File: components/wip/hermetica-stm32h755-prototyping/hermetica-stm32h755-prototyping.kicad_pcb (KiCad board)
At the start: 4 copper layers, 74.9 x 110.5 mm, 233 parts, among them J1 CONNECTOR-DEBUG-SPECIFIC-ARM, J10 Conn_01x01, J100 Conn_01x01, J101 Conn_01x01, J102 Conn_01x01, J103 Conn_01x01, J104 Conn_01x01, J105 Conn_01x01, J106 Conn_01x01, J107 Conn_01x01, J108 Conn_01x01, J109 Conn_01x01, J11 Conn_01x01, J111 Conn_01x01, J112 Conn_01x01, J113 Conn_01x01, J114 Conn_01x01, J115 Conn_01x01, J116 Conn_01x01, J117 Conn_01x01, J118 Conn_01x01, J119 Conn_01x01, J12 Conn_01x01, J120 Conn_01x01, J121 Conn_01x01, J122 Conn_01x01, J123 Conn_01x01, J124 Conn_01x01, J125 Conn_01x01, J126 Conn_01x01, J127 Conn_01x01, J128 Conn_01x01, J129 Conn_01x01, J13 Conn_01x01, J130 Conn_01x01, J131 Conn_01x01, J132 Conn_01x01, J133 Conn_01x01, J134 Conn_01x01, J135 Conn_01x01, J136 Conn_01x01, J137 Conn_01x01, J138 Conn_01x01, J139 Conn_01x01, J14 Conn_01x01, J140 Conn_01x01, J141 Conn_01x01, J142 Conn_01x01, J143 Conn_01x01, J144 Conn_01x01, J145 Conn_01x01, J146 Conn_01x01, J147 Conn_01x01, J148 Conn_01x01, J149 Conn_01x01, J15 Conn_01x01, J16 Conn_01x01, J17 Conn_01x01, J18 Conn_01x01, J19 Conn_01x01, J2 Conn_01x01, J20 Conn_01x01, J21 Conn_01x01, J22 Conn_01x01, J23 Conn_01x01, J24 Conn_01x01, J25 Conn_01x01, J26 Conn_01x01, J27 Conn_01x01, J28 Conn_01x01, J29 Conn_01x01, J3 Conn_01x01, J30 Conn_01x01, J31 Conn_01x01, J32 Conn_01x01, J33 Conn_01x01, J34 Conn_01x01, J35 Conn_01x01, J36 Conn_01x01, J37 Conn_01x01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

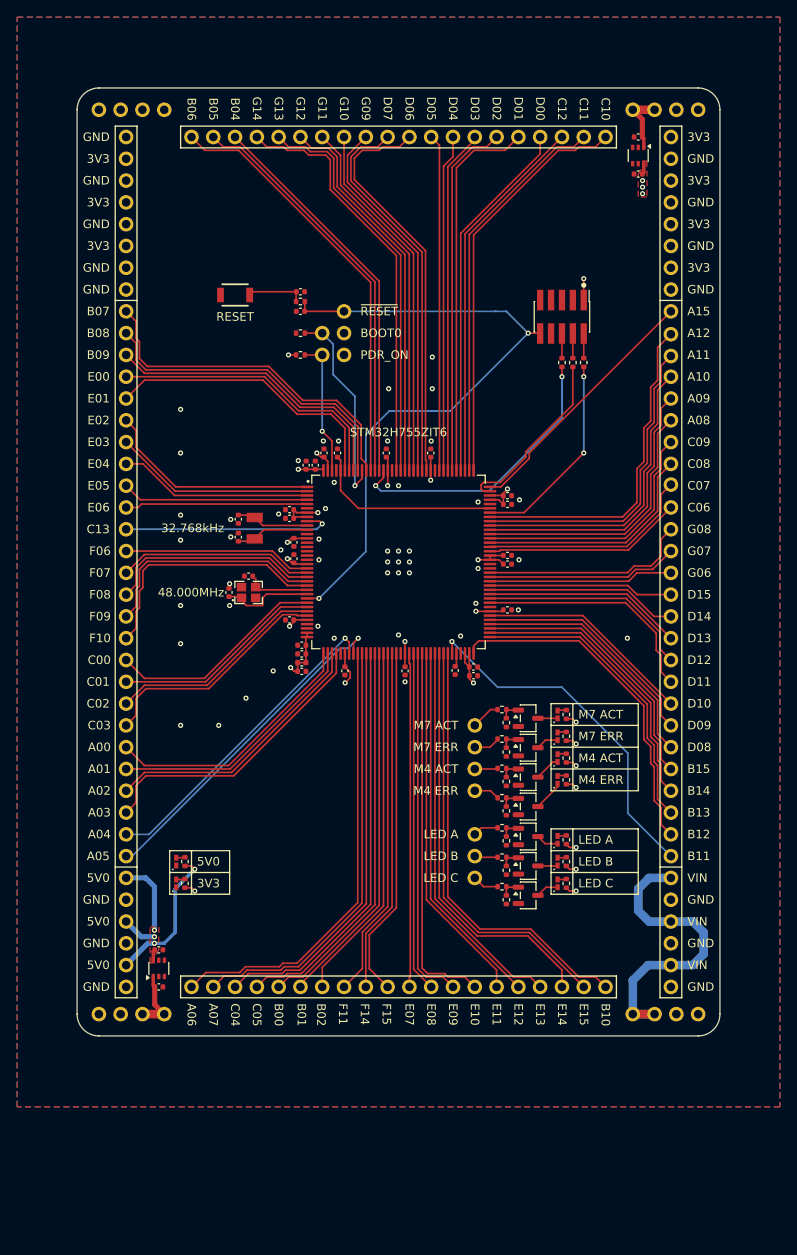
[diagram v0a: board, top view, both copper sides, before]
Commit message: STM32H755ZIT6 dev board
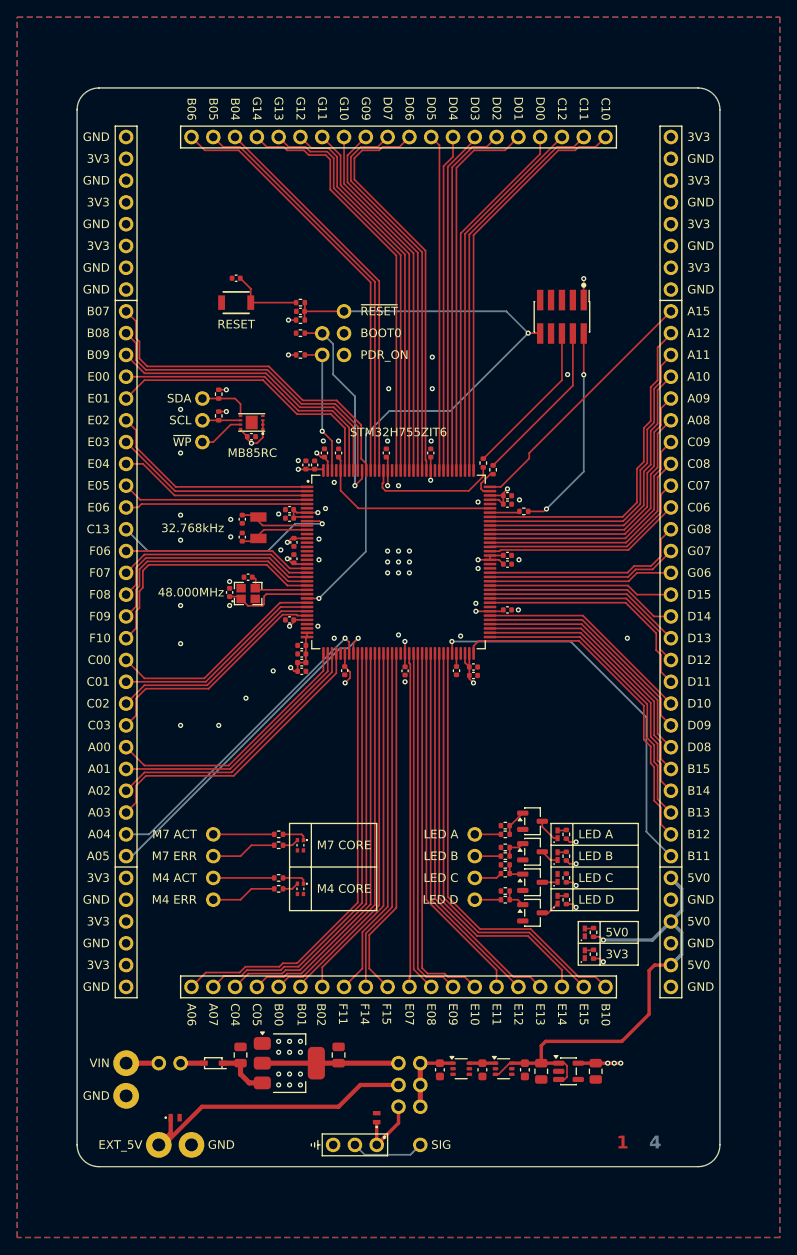
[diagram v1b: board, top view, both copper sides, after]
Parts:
- removed C39, C40, C41, C42: 100nF, djStandard:C_0402_1005Metric
- removed C43, C44, C45, C46: 2.2uF, djStandard:C_0402_1005Metric
- removed J10, J11, J12, J13, J14, J15, J16, J33, J36, J39, J7, J8, J9: Conn_01x01, djStandard:CONNECTOR-PCB-HANDSOLDER-01X01-FEMALE
- removed J143, J144, J145: Conn_01x01, djStandard:CONNECTOR-PCB-HANDSOLDER-01X01-MALE
- removed LED7, LED8, LED9: KINGBRIGHT-LED-0402-ORANGE, djStandard:KINGBRIGHT-LED-APHHS1005-0402
- removed Q5, Q6, Q7: DIODESINC-MMBT4401-7-F-SOT-23-3, Package_TO_SOT_SMD:SOT-23-3
- removed R24, R27: 47K, djStandard:R_0402_1005Metric
- removed R25, R28: 10K, djStandard:R_0402_1005Metric
- removed R26: ?, djStandard:R_0402_1005Metric
- removed R29: 22R, djStandard:R_0402_1005Metric
- removed U2: LM66100DCK, Package_TO_SOT_SMD:SOT-363_SC-70-6
- added C12: 4.7uF, djStandard:C_0402_1005Metric, F.Cu at (-10.8, -11.3)
- added C13: 100nF, djStandard:C_0402_1005Metric, F.Cu at (-8.64, -12.7)
- added C14: 100nF, djStandard:C_0402_1005Metric, F.Cu at (12.7, -6.73)
- added C15: 100nF, djStandard:C_0402_1005Metric, F.Cu at (12.7, 0.25)
- added C16: 100nF, djStandard:C_0402_1005Metric, F.Cu at (-6.27, 12.7)
- added C17: 100nF, djStandard:C_0402_1005Metric, F.Cu at (8.74, 13.2)
- added C18: 100nF, djStandard:C_0402_1005Metric, F.Cu at (-12.7, -5.11)
- added C3: 2.2uF, djStandard:C_0402_1005Metric, F.Cu at (-17.5, 1.78)
- added C6: 2.2uF, djStandard:C_0402_1005Metric, F.Cu at (-18.2, -2.90)
- added C7: 2.2uF, djStandard:C_0402_1005Metric, F.Cu at (6.76, 12.7)
- added C8: 2.2uF, djStandard:C_0402_1005Metric, F.Cu at (-6.99, -12.7)
- added C9: 10uF, djStandard:C_0402_1005Metric, F.Cu at (-11.3, 12.8)
- added D1: BAT60JFILM, djStandard:STM-BAT60JFILM-SOT-323-2, F.Cu at (-21.6, 58.4)
- added D2: ESDA7P60-1U1M, djStandard:STM-ESDA7P60-1U1M, F.Cu at (-2.54, 64.8)
- added D3: ESDA7P60-1U1M, djStandard:STM-ESDA7P60-1U1M, F.Cu at (-26.0, 64.8)
- added H1: MountingHole_Pad, djStandard:MountingHole_1.5mm, F.Cu at (-31.8, 58.4)
- added H2: MountingHole_Pad, djStandard:MountingHole_1.5mm, F.Cu at (-31.8, 62.2)
- added H3: MountingHole_Pad, djStandard:MountingHole_1.5mm, F.Cu at (-27.9, 67.9)
- added H4: MountingHole_Pad, djStandard:MountingHole_1.5mm, F.Cu at (-24.1, 67.9)
- added IC1: FUJITSU-MB85RC64TAPN, djStandard:FUJITSU-MB85RC64TAPN-SON8, F.Cu at (-17.1, -16.3)
- added J110: Conn_01x01, djStandard:CONNECTOR-PCB-HANDSOLDER-01X01-FEMALE, F.Cu at (-31.8, -11.4)
- added J150: Conn_01x01, djStandard:CONNECTOR-PCB-HANDSOLDER-01X01-FEMALE, F.Cu at (-21.6, 39.4)
- added J151: Conn_01x01, djStandard:CONNECTOR-PCB-HANDSOLDER-01X01-FEMALE, F.Cu at (-21.6, 36.8)
- added J70: Conn_01x01, djStandard:CONNECTOR-PCB-HANDSOLDER-01X01-FEMALE, F.Cu at (31.8, 34.3)
- added J71: Conn_01x01, djStandard:CONNECTOR-PCB-HANDSOLDER-01X01-FEMALE, F.Cu at (31.8, 31.8)
- added J72: Conn_01x01, djStandard:CONNECTOR-PCB-HANDSOLDER-01X01-FEMALE, F.Cu at (31.8, 29.2)
- added JP1: Jumper_2_Open, djStandard:CONNECTOR-PCB-HANDSOLDER-01X02-MALE, F.Cu at (-8.89, -24.1)
- added JP4: Jumper_2_Open, djStandard:CONNECTOR-PCB-HANDSOLDER-01X02-MALE, F.Cu at (0.00, 58.4)
- added JP5: Jumper_2_Open, djStandard:CONNECTOR-PCB-HANDSOLDER-01X02-MALE, F.Cu at (0.00, 61.0)
- added JP6: Jumper_2_Open, djStandard:CONNECTOR-PCB-HANDSOLDER-01X02-MALE, F.Cu at (0.00, 63.5)
- added LED10: APHB1608CGKSURKC, djStandard:KINGBRIGHT-APHB1608CGKSURKC, F.Cu at (-11.4, 33.0)
- added LED11: APHB1608CGKSURKC, djStandard:KINGBRIGHT-APHB1608CGKSURKC, F.Cu at (-11.4, 38.1)
- added R30: ?, djStandard:R_0402_1005Metric, F.Cu at (-14.0, 33.0)
- added R31: ?, djStandard:R_0402_1005Metric, F.Cu at (-14.0, 31.8)
- added R32: ?, djStandard:R_0402_1005Metric, F.Cu at (-14.0, 38.1)
- added R33: ?, djStandard:R_0402_1005Metric, F.Cu at (-14.0, 36.8)
- added U3: LM66100DCK, Package_TO_SOT_SMD:SOT-363_SC-70-6, F.Cu at (7.30, 59.1)
- added U4: LM66100DCK, Package_TO_SOT_SMD:SOT-363_SC-70-6, F.Cu at (12.3, 59.1)
- added U5: AP2112K-3.3, Package_TO_SOT_SMD:SOT-23-5, F.Cu at (19.8, 59.4)
- C1: value 1uF -> 22nF
- C10: value 10pF -> 1uF
- C11: value 22nF -> 100nF
- C2: value 1uF -> 10pF
- C31: value 4.7uF -> 10uF; footprint djStandard:C_0402_1005Metric -> djStandard:C_0805_2012Metric
- C32: value 100nF -> 10uF; footprint djStandard:C_0402_1005Metric -> djStandard:C_0805_2012Metric
- C34, C35, C36: value 100nF -> 1uF; footprint djStandard:C_0402_1005Metric -> djStandard:C_0603_1608Metric
- C37, C38: value 2.2uF -> 1uF; footprint djStandard:C_0402_1005Metric -> djStandard:C_0805_2012Metric
- C4, C5: value 1uF -> 2.2uF
- J1: value CONNECTOR-DEBUG-SPECIFIC-ARM -> Conn_01x01; footprint djStandard:PinHeader_2x05_P1.27mm_Vertical_SMD -> djStandard:CONNECTOR-PCB-HANDSOLDER-01X01-FEMALE
- J128, J129, J136, J137, J138, J139, J140, J141, J142, J147, J148, J149: footprint djStandard:CONNECTOR-PCB-HANDSOLDER-01X01-MALE -> djStandard:CONNECTOR-PCB-HANDSOLDER-01X01-FEMALE; moved to F.Cu
- J146: value Conn_01x01 -> DRONE-SERVO-HEADER; footprint djStandard:CONNECTOR-PCB-HANDSOLDER-01X01-MALE -> djStandard:CONNECTOR-SERVO-VERTICAL; moved to F.Cu
- J17: value Conn_01x01 -> CONNECTOR-DEBUG-SPECIFIC-ARM; footprint djStandard:CONNECTOR-PCB-HANDSOLDER-01X01-FEMALE -> djStandard:PinHeader_2x05_P1.27mm_Vertical_SMD
- LED2: value KINGBRIGHT-LED-0402-RED -> KINGBRIGHT-LED-0402-ORANGE
- LED6: value KINGBRIGHT-LED-0402-ORANGE -> KINGBRIGHT-LED-0402-RED
- R1, R3: value ? -> 22R
- R10: value 1K -> ?
- R12, R7: value 47K -> ?
- R13, R16: value 10K -> 47K
- R14: value ? -> 47K
- R17, R20: value ? -> 10K
- R18, R21: value 47K -> 10K
- R22: value 10K -> 20K
- R23: value ? -> 20K
- R4: value 22R -> 10K
- R6: value ? -> 1K
- R8, R9: value 10K -> ?
- SW1: value OMRON-B3U-1000PM -> B3U1000PM
- U1: value LM66100DCK -> LD1117S50TR_SOT223; footprint Package_TO_SOT_SMD:SOT-363_SC-70-6 -> Package_TO_SOT_SMD:SOT-223-3_TabPin2
- Y1: value ABRACON-ABS07-LR-32.768KHZ-6-1-T -> ABRACON-ABM10AIG-48.000MHZ-4Z-T3; footprint djStandard:ABRACON-ABS07-LR -> djStandard:ABRACON-ABM10AIG
- Y2: value ABRACON-ABM10AIG-48.000MHZ-4Z-T3 -> ABRACON-ABS07-LR-32.768KHZ-6-1-T; footprint djStandard:ABRACON-ABM10AIG -> djStandard:ABRACON-ABS07-LR
- moved J147 125.6 mm to (2.54, 67.9), turned to 0 degrees
- moved J146 124.9 mm to (-2.54, 67.9), turned to -90 degrees
- moved U1 113.3 mm to (-12.7, 58.4), turned to 0 degrees
- moved J138 112.3 mm to (-16.5, -49.5), turned to 0 degrees
- moved J136 109.3 mm to (-11.4, -49.5), turned to 0 degrees
- moved J128 109.3 mm to (-3.81, 49.5), turned to 0 degrees
- moved J129 107.6 mm to (-1.27, 49.5), turned to 0 degrees
- moved J119 104.4 mm to (16.5, 49.5)
- moved J118 102.9 mm to (14.0, 49.5)
- moved J117 101.7 mm to (11.4, 49.5)
- moved J121 101.5 mm to (21.6, 49.5)
- moved J60 101.2 mm to (31.8, -39.4)
- moved J116 100.6 mm to (8.89, 49.5)
- moved J115 99.9 mm to (6.35, 49.5)
- moved J97 99.6 mm to (-1.27, -49.5), turned to 0 degrees
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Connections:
- C1 pad 1: /EXT_3V3 -> /mcu/RESET
- C10 pad 1: Net-(C10-Pad1) -> +3V3
- C11 pad 1: /mcu/RESET -> +3V3
- C2 pad 1: /EXT_5V0 -> Net-(C2-Pad1)
- C31 pad 1: +3V3 -> Net-(D1-K)
- C32 pad 1: +3V3 -> Net-(JP4-A)
- C34 pad 1: +3V3 -> 5V_PREDIODE
- C35 pad 1: +3V3 -> Net-(U3-VOUT)
- C36 pad 1: +3V3 -> +5V0
- C37 pad 1: /mcu/VCAP2 -> +5V0
- C38 pad 1: /mcu/VCAP1 -> +3V3
- C4 pad 1: +3V3 -> GND
- C4 pad 2: GND -> Net-(MCU1-OSC_HSE-)
- C5 pad 1: +5V0 -> GND
- C5 pad 2: GND -> Net-(MCU1-OSC_LSE+)
- J1 pad 1: +3V3 -> /mcu/SCL
- J100 pad 1: /mcu/PE13 -> /mcu/PD10
- J101 pad 1: /mcu/PE14 -> /mcu/PD11
- J102 pad 1: /mcu/PE15 -> /mcu/PD12
- J103 pad 1: /mcu/PF06 -> /mcu/PD13
- J104 pad 1: /mcu/PF07 -> /mcu/PD14
- J105 pad 1: /mcu/PF08 -> /mcu/PD15
- J106 pad 1: /mcu/PF09 -> /mcu/PE00
- J107 pad 1: /mcu/PF10 -> /mcu/PE01
- J108 pad 1: /mcu/PF11 -> /mcu/PE02
- J109 pad 1: GND -> /mcu/PE03
- J111 pad 1: /mcu/PG06 -> /mcu/PE05
- J112 pad 1: /mcu/PG07 -> /mcu/PE06
- J113 pad 1: /mcu/PG08 -> /mcu/PE07
- J114 pad 1: /mcu/PG09 -> /mcu/PE08
- J115 pad 1: /mcu/PG10 -> /mcu/PE09
- J116 pad 1: /mcu/PG11 -> /mcu/PE10
- J117 pad 1: /mcu/PG12 -> /mcu/PE11
- J118 pad 1: /mcu/PG13 -> /mcu/PE12
- J119 pad 1: /mcu/PG14 -> /mcu/PE13
- J120 pad 1: /mcu/PA12 -> /mcu/PE14
- J121 pad 1: +3V3 -> /mcu/PE15
- J122 pad 1: GND -> /mcu/PF06
- J123 pad 1: +3V3 -> /mcu/PF07
- J124 pad 1: GND -> /mcu/PF08
- J125 pad 1: GND -> /mcu/PF09
- J126 pad 1: +3V3 -> /mcu/PF10
- J127 pad 1: GND -> /mcu/PF11
- J128 pad 1: GND -> /mcu/PF14
- J129 pad 1: GND -> /mcu/PF15
- J130 pad 1: +5V0 -> /mcu/PG06
- J131 pad 1: +5V0 -> /mcu/PG07
- J132 pad 1: GND -> /mcu/PG08
- J133 pad 1: GND -> /mcu/PG09
- J134 pad 1: GND -> /mcu/PG10
- J135 pad 1: +5V0 -> /mcu/PG11
- J136 pad 1: EXT_VIN -> /mcu/PG12
- J137 pad 1: /EXT_3V3 -> /mcu/PG13
- J138 pad 1: EXT_VIN -> /mcu/PG14
- J139 pad 1: /EXT_3V3 -> /leds/LED_A
- J140 pad 1: GND -> /leds/LED_B
- J141 pad 1: GND -> /leds/LED_C
- J142 pad 1: GND -> /leds/LED_D
- J146 pad 1: GND -> /power/BEC_5V
- J147 pad 1: GND -> /power/BEC_SIGNAL
- J148 pad 1: unconnected-(J148-Pin_1-Pad1) -> /leds/M7_RED
- J149 pad 1: unconnected-(J149-Pin_1-Pad1) -> /leds/M7_GRN
- J17 pad 1: /mcu/PD01 -> +3V3
- J18 pad 1: /mcu/PD00 -> /mcu/PA00
- J19 pad 1: EXT_VIN -> +5V0
- J2 pad 1: /mcu/RESET -> /mcu/SDA
- J20 pad 1: GND -> /mcu/PA01
- J21 pad 1: +3V3 -> +5V0
- J22 pad 1: /mcu/PF14 -> /mcu/PA02
- J23 pad 1: /mcu/PF15 -> +5V0
- J24 pad 1: /mcu/PA00 -> /mcu/PA03
- J25 pad 1: /mcu/PA01 -> /mcu/PA04
- J26 pad 1: /mcu/PA02 -> /mcu/PA05
- J27 pad 1: /mcu/PA03 -> /mcu/PA06
- J28 pad 1: Net-(J28-Pin_1) -> GND
- J29 pad 1: Net-(J29-Pin_1) -> /mcu/PA07
- J3 pad 1: Net-(J3-Pin_1) -> Net-(IC1-WP)
- J30 pad 1: /mcu/PA06 -> GND
- J31 pad 1: /mcu/PA07 -> /mcu/PA08
- J32 pad 1: /mcu/PA08 -> GND
- J34 pad 1: /mcu/PA10 -> /mcu/PA09
- J35 pad 1: /mcu/PB12 -> GND
- J37 pad 1: GND -> /mcu/PA10
- J38 pad 1: /mcu/PB07 -> GND
- J4 pad 1: EXT_VIN -> +3V3
- J40 pad 1: /mcu/PB00 -> /mcu/PA11
- J41 pad 1: /mcu/PB01 -> GND
- J42 pad 1: /mcu/PB02 -> /mcu/PA12
- J43 pad 1: /mcu/PB04 -> GND
- J44 pad 1: /mcu/PB13 -> GND
- J46 pad 1: Net-(J46-Pin_1) -> +3V3
- J47 pad 1: /mcu/PB08 -> /mcu/PA15
- J48 pad 1: /mcu/PB09 -> GND
- J49 pad 1: /mcu/PB10 -> +3V3
- J5 pad 1: EXT_VIN -> +3V3
- J50 pad 1: /mcu/PB11 -> GND
- J51 pad 1: Net-(J51-Pin_1) -> +3V3
- J52 pad 1: Net-(J52-Pin_1) -> /mcu/PB00
- J53 pad 1: /mcu/PB14 -> GND
- J54 pad 1: /mcu/PB15 -> +3V3
- J55 pad 1: /mcu/PC00 -> /mcu/PB01
- J56 pad 1: /mcu/PC01 -> GND
- J57 pad 1: /mcu/PC02 -> +3V3
- J58 pad 1: /mcu/PC03 -> /mcu/PB02
- J59 pad 1: /mcu/PC04 -> GND
- J6 pad 1: /mcu/PA04 -> +3V3
- J60 pad 1: /mcu/PC05 -> +3V3
- J61 pad 1: /mcu/PC06 -> /mcu/PB04
- J62 pad 1: /mcu/PC07 -> GND
- J63 pad 1: /mcu/PC08 -> +3V3
- J64 pad 1: /mcu/PC09 -> /mcu/PB05
- J65 pad 1: /mcu/PC10 -> /mcu/PB06
- J66 pad 1: /mcu/PC11 -> /mcu/PB07
- J67 pad 1: /mcu/PC12 -> /mcu/PB08
- J68 pad 1: /mcu/PC13 -> /mcu/PB09
- J69 pad 1: +3V3 -> /mcu/PB10
- J73 pad 1: /mcu/PD02 -> /mcu/PB14
- J74 pad 1: /mcu/PD03 -> /mcu/PB15
- J75 pad 1: /mcu/PD04 -> /mcu/PC00
- J76 pad 1: /mcu/PD05 -> /mcu/PC01
- J77 pad 1: /mcu/PD06 -> /mcu/PC02
- J78 pad 1: /mcu/PD07 -> /mcu/PC03
- J79 pad 1: /mcu/PD08 -> /mcu/PC04
- J80 pad 1: /mcu/PD09 -> /mcu/PC05
- J81 pad 1: /mcu/PD10 -> /mcu/PC06
- J82 pad 1: /mcu/PD11 -> /mcu/PC07
- J83 pad 1: /mcu/PD12 -> /mcu/RESET
- J84 pad 1: /mcu/PD13 -> /mcu/PC08
- J85 pad 1: /mcu/PD14 -> /mcu/PC09
- J86 pad 1: /mcu/PD15 -> /mcu/PC10
- J87 pad 1: /mcu/PE00 -> /mcu/PC11
- J88 pad 1: /mcu/PE01 -> /mcu/PC12
- J89 pad 1: /mcu/PE02 -> /mcu/PC13
- J90 pad 1: /mcu/PE03 -> /mcu/PD00
- J91 pad 1: /mcu/PE04 -> /mcu/PD01
- J92 pad 1: /mcu/PE05 -> /mcu/PD02
- J93 pad 1: /mcu/PE06 -> /mcu/PD03
- J94 pad 1: /mcu/PE07 -> /mcu/PD04
- J95 pad 1: /mcu/PE08 -> /mcu/PD05
- J96 pad 1: /mcu/PE09 -> /mcu/PD06
- J97 pad 1: /mcu/PE10 -> /mcu/PD07
- J98 pad 1: /mcu/PE11 -> /mcu/PD08
- J99 pad 1: /mcu/PE12 -> /mcu/PD09
- JP2 pad 1: /mcu/PDR_ON -> /mcu/BOOT0
- JP2 pad 2: GND -> +3V3
- JP3 pad 1: /mcu/BOOT0 -> /power/VIN
- JP3 pad 2: +3V3 -> Net-(D1-A)
- LED1 pad 1: Net-(LED1-K) -> GND
- LED2 pad 1: Net-(LED2-K) -> GND
- LED6 pad 1: GND -> Net-(LED6-K)
- Q1 pad 3: Net-(LED1-K) -> Net-(LED3-K)
- Q2 pad 3: Net-(LED2-K) -> Net-(LED4-K)
- Q3 pad 3: Net-(LED3-K) -> Net-(LED5-K)
- Q4 pad 3: Net-(LED4-K) -> Net-(LED6-K)
- R1 pad 1: Net-(LED1-A) -> /mcu/SWCLK
- R1 pad 2: +3V3 -> Net-(MCU1-SWCLK)
- R10 pad 1: /mcu/RESET -> Net-(LED4-A)
- R10 pad 2: Net-(C10-Pad1) -> +3V3
- R11 pad 1: Net-(LED2-A) -> Net-(LED5-A)
- R12 pad 1: Net-(Q2-B) -> Net-(LED6-A)
- R12 pad 2: Net-(J9-Pin_1) -> +3V3
- R13 pad 1: GND -> Net-(Q1-B)
- R13 pad 2: Net-(Q2-B) -> /leds/LED_A
- R14 pad 1: Net-(LED3-A) -> Net-(Q2-B)
- R14 pad 2: +3V3 -> /leds/LED_B
- R15 pad 2: Net-(J28-Pin_1) -> /leds/LED_C
- R16 pad 1: GND -> Net-(Q4-B)
- R16 pad 2: Net-(Q3-B) -> /leds/LED_D
- R17 pad 1: Net-(LED4-A) -> GND
- R17 pad 2: +3V3 -> Net-(Q1-B)
- R18 pad 1: Net-(Q4-B) -> GND
- R18 pad 2: Net-(J29-Pin_1) -> Net-(Q2-B)
- R19 pad 2: Net-(Q4-B) -> Net-(Q3-B)
- R2 pad 1: /mcu/SWCLK -> /mcu/SWDIO
- R2 pad 2: Net-(MCU1-SWCLK) -> Net-(MCU1-SWDIO)
- R20 pad 1: Net-(LED5-A) -> GND
- R20 pad 2: +3V3 -> Net-(Q4-B)
- R21 pad 1: Net-(Q5-B) -> +3V3
- R21 pad 2: Net-(J46-Pin_1) -> /mcu/RESET
- R22 pad 1: GND -> +3V3
- R22 pad 2: Net-(Q5-B) -> /mcu/SCL
- R23 pad 1: Net-(LED8-A) -> +3V3
- R23 pad 2: +3V3 -> /mcu/SDA
- R3 pad 1: Net-(LED6-A) -> /mcu/SWO
- R3 pad 2: +5V0 -> Net-(MCU1-SWO)
- R4 pad 1: /mcu/SWDIO -> +3V3
- R4 pad 2: Net-(MCU1-SWDIO) -> /mcu/PDR_ON
- R5 pad 1: GND -> /mcu/BOOT0
- R5 pad 2: Net-(Q1-B) -> GND
- R6 pad 1: Net-(LED7-A) -> /mcu/RESET
- R6 pad 2: +3V3 -> Net-(C2-Pad1)
- R7 pad 1: Net-(Q1-B) -> Net-(LED1-A)
- R7 pad 2: Net-(J3-Pin_1) -> +5V0
- R8 pad 1: +3V3 -> Net-(LED2-A)
- R8 pad 2: /mcu/PDR_ON -> +3V3
- R9 pad 1: /mcu/BOOT0 -> Net-(LED3-A)
- R9 pad 2: GND -> +3V3
- SW1 pad 1: Net-(C10-Pad1) -> Net-(C2-Pad1)
- U1 pad 1: /EXT_3V3 -> GND
- U1 pad 2: GND -> Net-(JP4-A)
- U1 pad 3: GND -> Net-(D1-K)
- Y1 pad 1: Net-(MCU1-OSC_LSE+) -> Net-(MCU1-OSC_HSE-)
- Y1 pad 2: Net-(MCU1-OSC_LSE-) -> GND
- Y2 pad 1: Net-(MCU1-OSC_HSE-) -> Net-(MCU1-OSC_LSE+)
- Y2 pad 2: GND -> Net-(MCU1-OSC_LSE-)
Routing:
- net EXT_VIN: track 36.6 -> 0.00 mm
- net /power/EXT_5V: track 0.00 -> 34.6 mm
- net +5V0: track 31.0 -> 57.7 mm, vias 4 -> 1
- net /mcu/SWDIO: track 2.87 -> 24.1 mm, vias 0 -> 2
- net Net-(MCU1-SWDIO): track 23.8 -> 3.29 mm, vias 2 -> 0
- net Net-(MCU1-SWO): track 33.6 -> 15.7 mm, vias 2 -> 0
- net Net-(MCU1-SWCLK): track 20.9 -> 3.63 mm
- net /mcu/SWCLK: track 2.87 -> 19.2 mm
- net Net-(JP4-A): track 0.00 -> 15.9 mm
- net /mcu/SWO: track 2.88 -> 18.4 mm
- net 5V_PREDIODE: track 0.00 -> 8.89 mm
- net Net-(C2-Pad1): track 0.00 -> 8.66 mm
- net /power/BEC_SIGNAL: track 0.00 -> 8.57 mm
- net +3V3: track 72.1 -> 80.3 mm, vias 28 -> 29
- net /power/BEC_5V: track 0.00 -> 8.15 mm
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- removed copper zone on F.Cu, net +3V3
- removed copper zone on F.Cu, net +5V0
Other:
- board size 74.9 x 110.5 mm -> 74.9 x 125.7 mm
- board text added: "1"
- board text added: "2"
- board text added: "3"
- board text added: "4"
- board text added: "EXT_5V"
- board text added: "LED D"
- board text added: "M4 CORE"
- board text added: "M7 CORE"
- board text added: "MB85RC"
- board text added: "SCL"
- board text added: "SDA"
- board text added: "SIG"
- board text added: "~{WP}"
